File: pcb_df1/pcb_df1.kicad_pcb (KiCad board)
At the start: 2 copper layers, 14.5 x 42.7 mm, 6 parts, among them J1 Cable, J2 Floppy, Q1 DMG2301L, Q2 BSS123

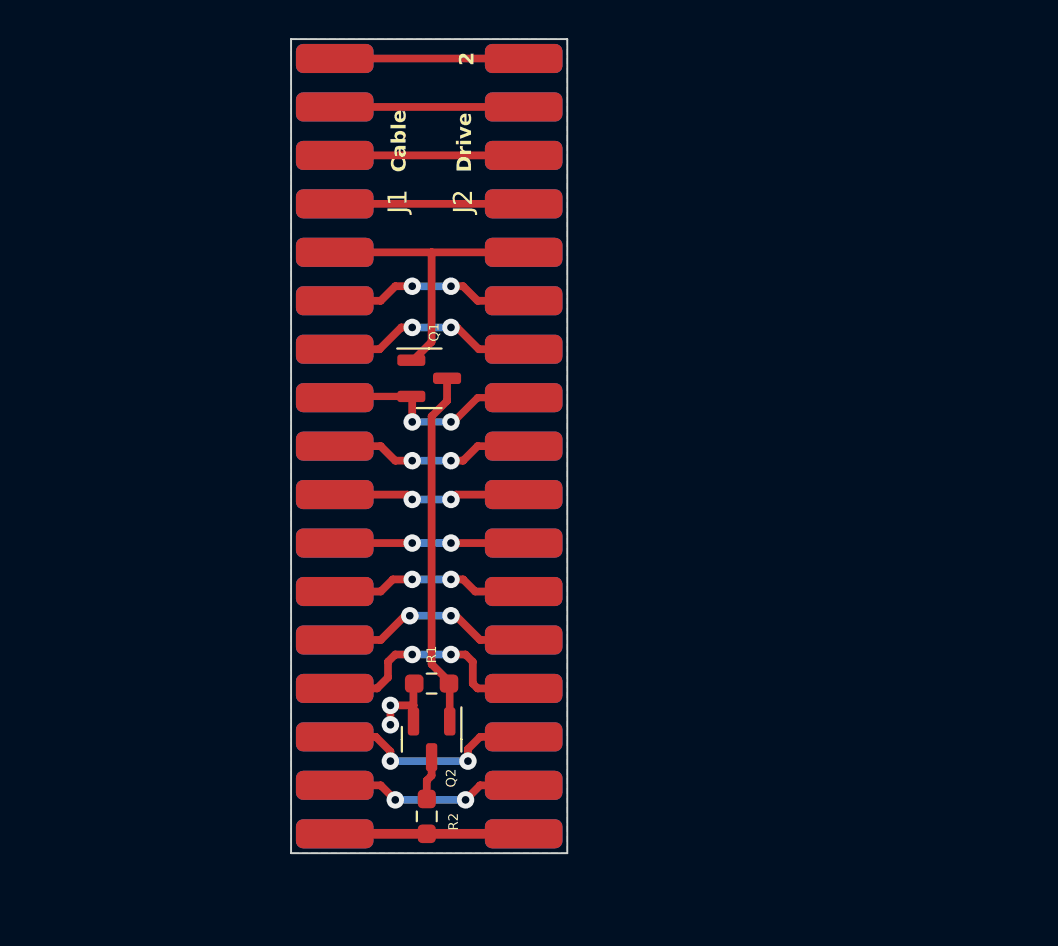
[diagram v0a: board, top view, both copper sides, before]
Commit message: pcb_df1: changed orinetation
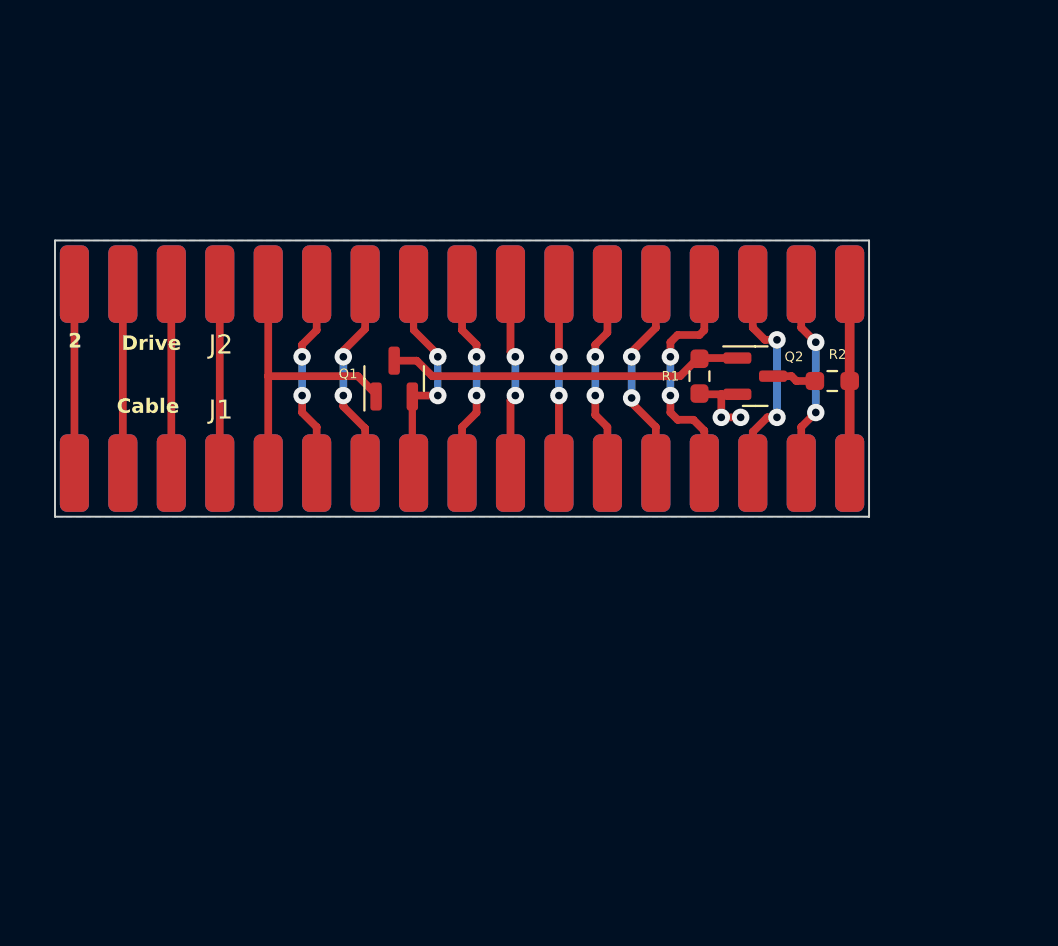
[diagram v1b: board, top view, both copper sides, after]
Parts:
- moved R2 31.2 mm to (145.7, 76.6), turned to 0 degrees
- moved J2 26.4 mm to (106.0, 71.5), turned to -90 degrees
- moved J1 25.7 mm to (106.0, 81.4), turned to -90 degrees
- moved Q2 25.5 mm to (141.7, 76.3), turned to 0 degrees
- moved R1 21.4 mm to (138.8, 76.3), turned to -90 degrees
- moved Q1 1.83 mm to (122.8, 76.5), turned to 90 degrees
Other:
- board size 14.5 x 42.7 mm -> 42.7 x 14.5 mm

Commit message: DF1 board reworked
New version sits on the other end of the flat cable.
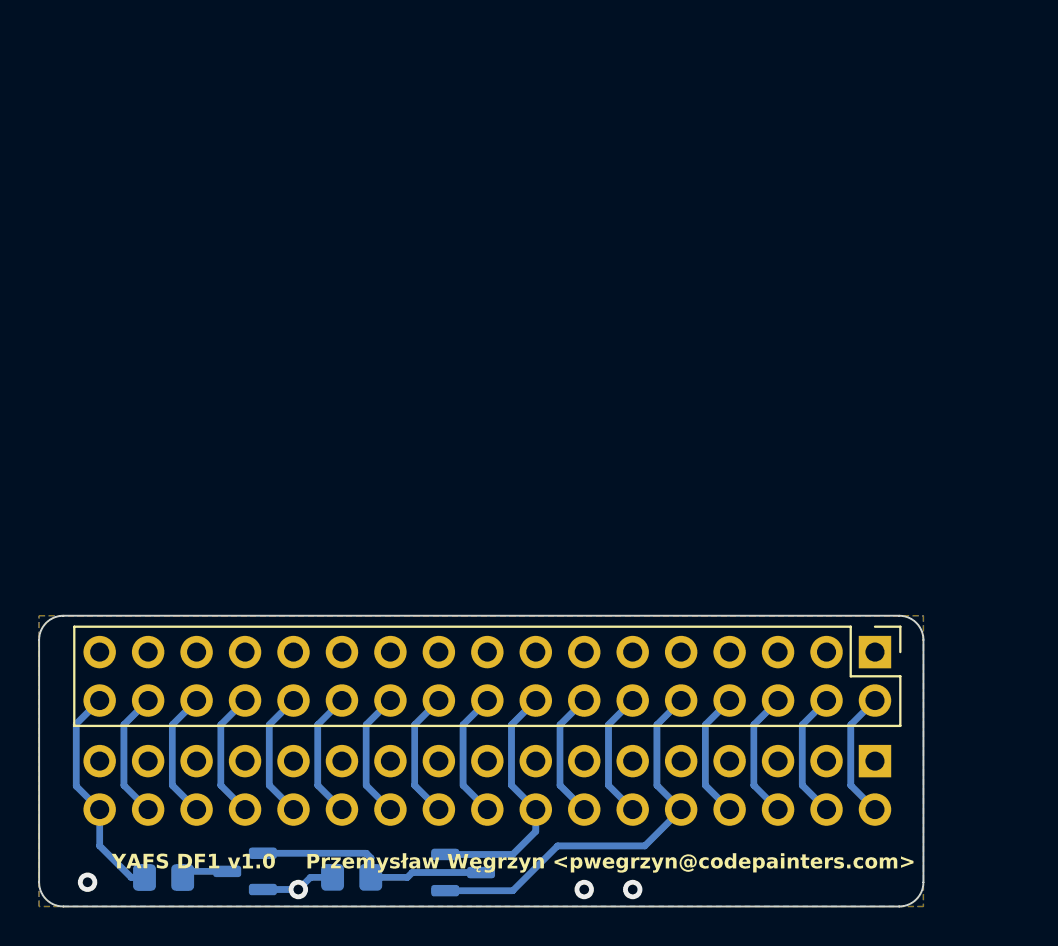
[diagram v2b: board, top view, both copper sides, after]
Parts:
- J1: value Cable -> MBoard; footprint pcb_df1:idc34_edge -> Connector_PinSocket_2.54mm:PinSocket_2x17_P2.54mm_Vertical
- J2: footprint pcb_df1:idc34_edge -> Connector_PinHeader_2.54mm:PinHeader_2x17_P2.54mm_Vertical; moved to F.Cu
- Q1, Q2: moved to B.Cu
- R1, R2: footprint Resistor_SMD:R_0603_1608Metric_Pad0.98x0.95mm_HandSolder -> Resistor_SMD:R_0805_2012Metric_Pad1.20x1.40mm_HandSolder; moved to B.Cu
- moved J2 46.2 mm to (148.0, 90.8)
- moved J1 44.6 mm to (148.0, 96.5), turned to 90 degrees
- moved R2 43.7 mm to (110.7, 102.6), turned to 180 degrees
- moved Q2 37.3 mm to (114.9, 102.3), turned to 180 degrees
- moved R1 32.0 mm to (120.5, 102.6), turned to 180 degrees
- moved Q1 26.1 mm to (126.4, 102.4), turned to 0 degrees
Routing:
- net Net-(Q1-D): track 18.7 -> 12.7 mm
- net Net-(J1-Pin_28): track 12.5 -> 6.77 mm, vias 2 -> 0
- net Net-(J1-Pin_30): track 11.6 -> 6.77 mm, vias 2 -> 0
- net /~{SEL0}: track 16.3 -> 20.9 mm
- net Net-(J1-Pin_14): track 10.9 -> 6.77 mm, vias 2 -> 0
- net Net-(J1-Pin_26): track 10.7 -> 6.77 mm, vias 2 -> 0
- net Net-(J1-Pin_12): track 10.5 -> 6.77 mm, vias 2 -> 0
- net Net-(J1-Pin_18): track 10.5 -> 6.77 mm, vias 2 -> 0
- net Net-(J1-Pin_32): track 10.3 -> 6.77 mm, vias 2 -> 0
- net Net-(J1-Pin_24): track 10.2 -> 6.77 mm, vias 2 -> 0
- net Net-(J1-Pin_4): track 9.91 -> 6.77 mm
- net Net-(J1-Pin_8): track 9.91 -> 6.77 mm
- net Net-(J1-Pin_6): track 9.91 -> 6.77 mm
- net Net-(J1-Pin_2): track 9.91 -> 6.77 mm
- net Net-(J1-Pin_20): track 9.86 -> 6.77 mm, vias 2 -> 0
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- added copper zone on F.Cu, net GND
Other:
- board size 42.7 x 14.5 mm -> 46.4 x 15.2 mm
- board text added: "Przemysław Węgrzyn <pwegrzyn@codepainters.com>"
- board text added: "YAFS DF1 v1.0"
- board text removed: "1"
- board text removed: "2"
- board text removed: "33"
- board text removed: "Cable"
- board text removed: "Drive"
- board text removed: "YAFS v1.0"

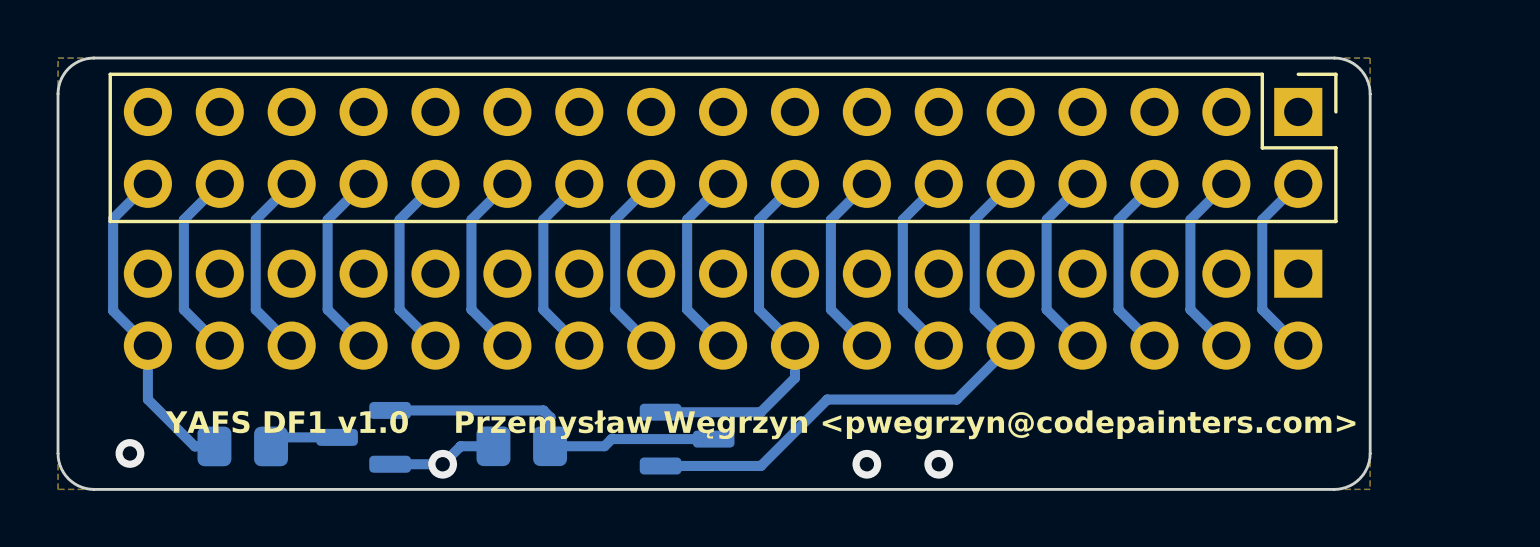
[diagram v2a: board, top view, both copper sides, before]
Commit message: DF1: GND fills reworked
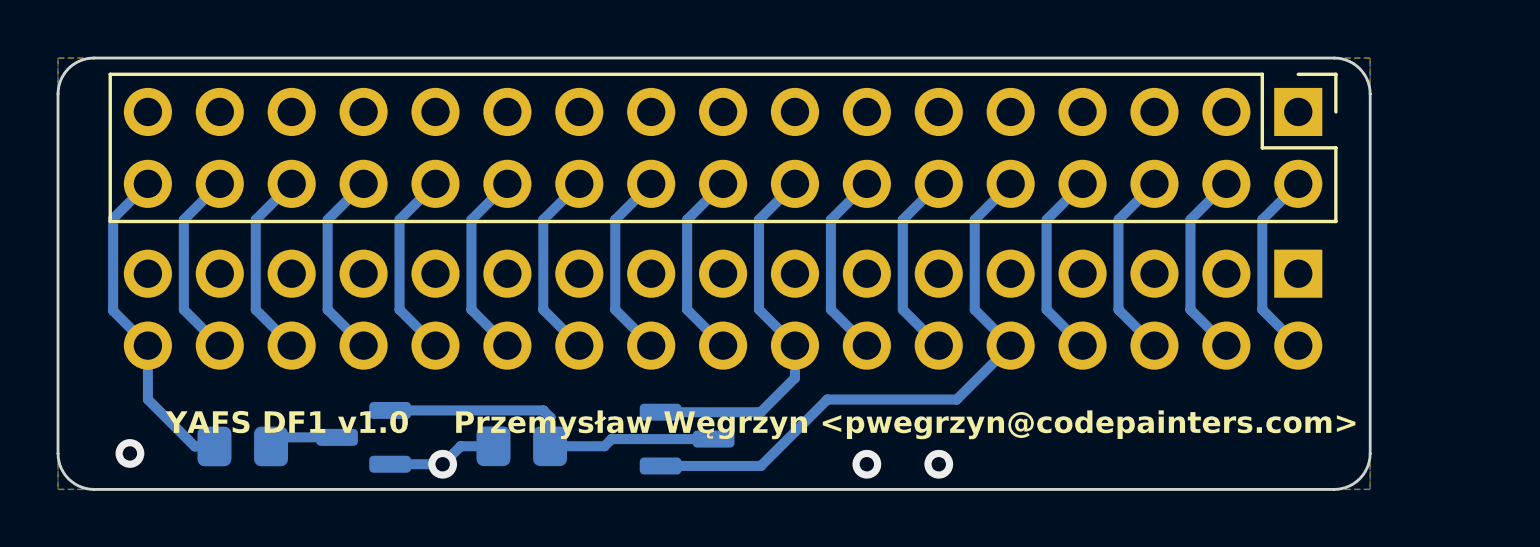
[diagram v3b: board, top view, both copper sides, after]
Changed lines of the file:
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@@
   (segment (start 108.585 94.615) (end 109.855 93.345) (width 0.3556) (layer "B.Cu") (net 20))
   (segment (start 109.855 99.06) (end 108.585 97.79) (width 0.3556) (layer "B.Cu") (net 20))
-  (zone (net 4) (net_name "GND") (layers "F&B.Cu") (hatch edge 0.5)
-    (connect_pads (clearance 0.3302))
+  (zone (net 4) (net_name "GND") (layer "F.Cu") (hatch edge 0.5)
+    (connect_pads (clearance 0.2794))
     (min_thickness 0.25) (filled_areas_thickness no)
-    (fill yes (thermal_gap 0.5) (thermal_bridge_width 0.5))
+    (fill yes (thermal_gap 0.2794) (thermal_bridge_width 0.2794))
     (polygon
       (pts
@@
       )
     )
+  )
+  (zone (net 4) (net_name "GND") (layer "B.Cu") (hatch edge 0.5)
+    (priority 1)
+    (connect_pads (clearance 0.3048))
+    (min_thickness 0.25) (filled_areas_thickness no)
+    (fill yes (thermal_gap 0.3048) (thermal_bridge_width 0.3048))
+    (polygon
+      (pts
+        (xy 104.14 88.9)
+        (xy 104.14 104.14)
+        (xy 150.495 104.14)
+        (xy 150.495 88.9)
+      )
+    )

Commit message: DF1: R1 value fixed
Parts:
- R1: value 10k -> 2k2
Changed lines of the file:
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@@
         (effects (font (size 0.508 0.508) (thickness 0.0762)) (justify mirror))
     )
-    (fp_text value "10k" (at 0 -1.65 -360) (layer "B.Fab") hide
+    (fp_text value "2k2" (at 0 -1.65 -360) (layer "B.Fab") hide
         (effects (font (size 1 1) (thickness 0.15)) (justify mirror))
     )
